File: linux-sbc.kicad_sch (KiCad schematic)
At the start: 10 parts, among them J101 Molex Mini-fit Jr

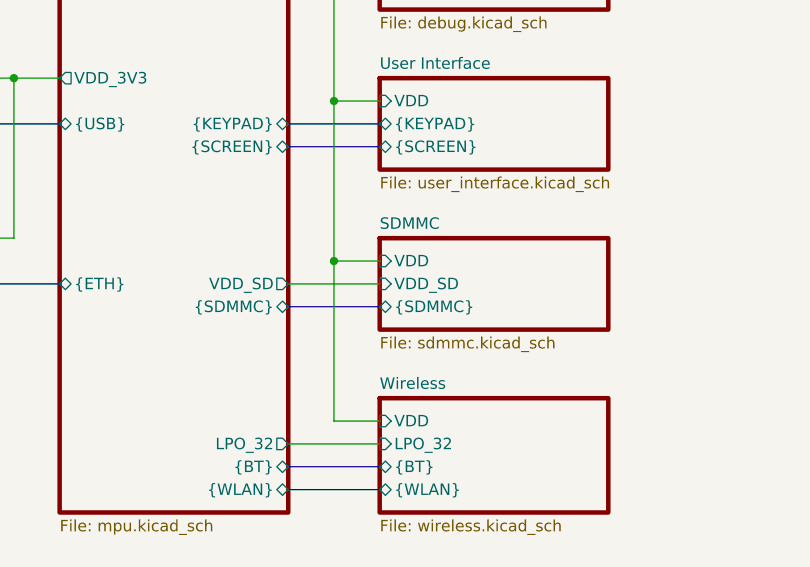
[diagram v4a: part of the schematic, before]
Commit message: Redo MPU pinout using STM32CubeMx
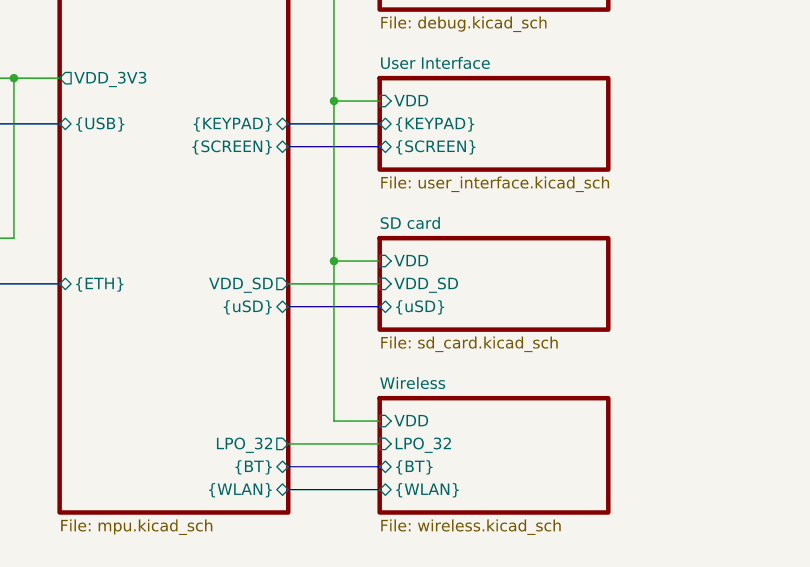
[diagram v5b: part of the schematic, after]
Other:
- sheet SDMMC renamed SD card
- sheet MPU ports: added {uSD}; removed {SDMMC}
- sheet SD card: file sdmmc.kicad_sch -> sd_card.kicad_sch
- sheet SD card ports: added {uSD}; removed {SDMMC}
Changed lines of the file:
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@@
 		(rev "v0.0.1")
 	)
-	(bus_alias "SDMMC"
-		(members "SDMMC.D[0..3]" "SDMMC.CMD" "SDMMC.CLK" "SDMMC.DET_N")
+	(bus_alias "uSD"
+		(members "uSD.D[0..3]" "uSD.CMD" "uSD.CLK" "uSD.DET_N")
 	)
 	(text "7. USB"
@@
 			(color 0 255 0 1.0000)
 		)
-		(property "Sheetname" "SDMMC"
+		(property "Sheetname" "SD card"
 			(at 252.73 165.4846 0)
 			(effects
@@
 			)
 		)
-		(property "Sheetfile" "sdmmc.kicad_sch"
+		(property "Sheetfile" "sd_card.kicad_sch"
 			(at 252.73 177.2884 0)
 			(effects
@@
 			)
 		)
-		(pin "{SDMMC}" bidirectional
+		(pin "{uSD}" bidirectional
 			(at 252.73 173.99 180)
 			(effects
@@
 			)
 		)
-		(pin "{SDMMC}" bidirectional
+		(pin "{uSD}" bidirectional
 			(at 242.57 173.99 0)
 			(effects

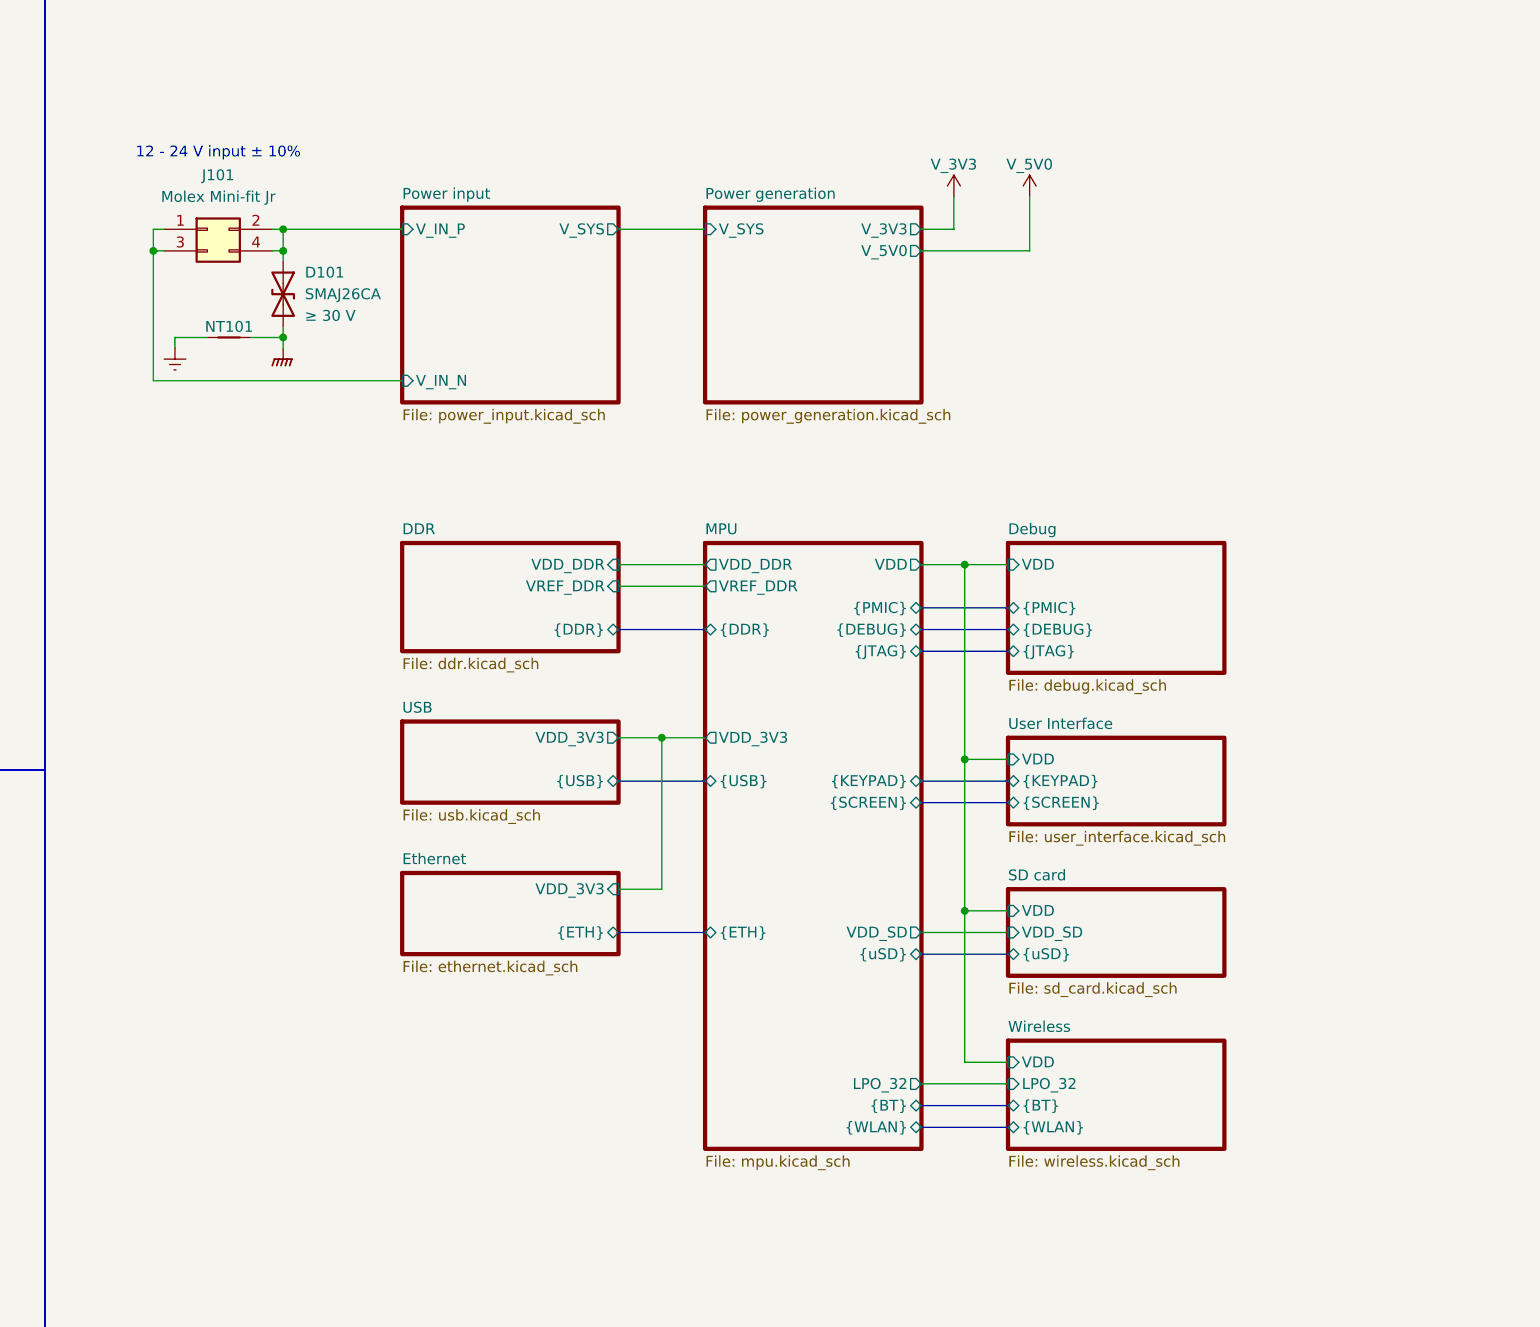
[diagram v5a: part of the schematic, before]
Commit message: Bridge chassis and gnd with 0 ohm
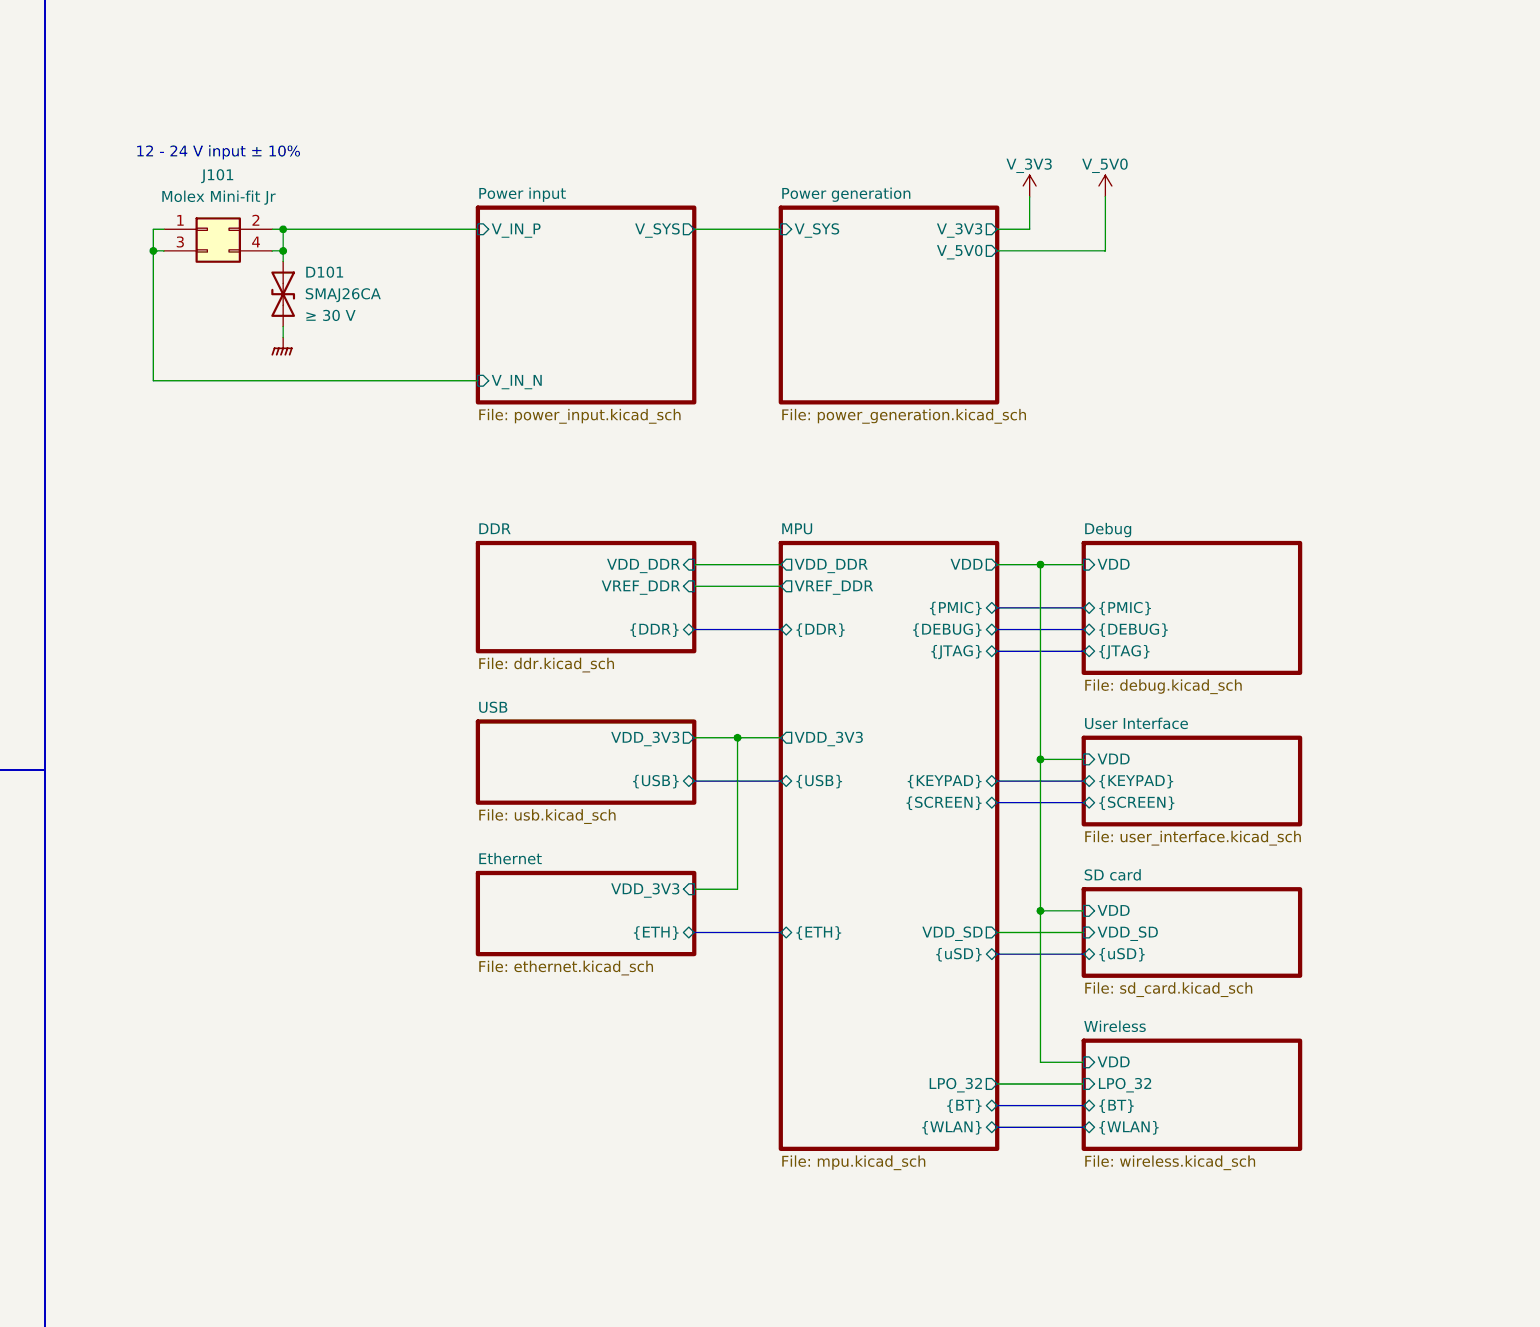
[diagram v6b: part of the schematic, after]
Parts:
- removed NT101: NetTie_2, NetTie:NetTie-2_SMD_Pad2.0mm, symbol Device:NetTie_2

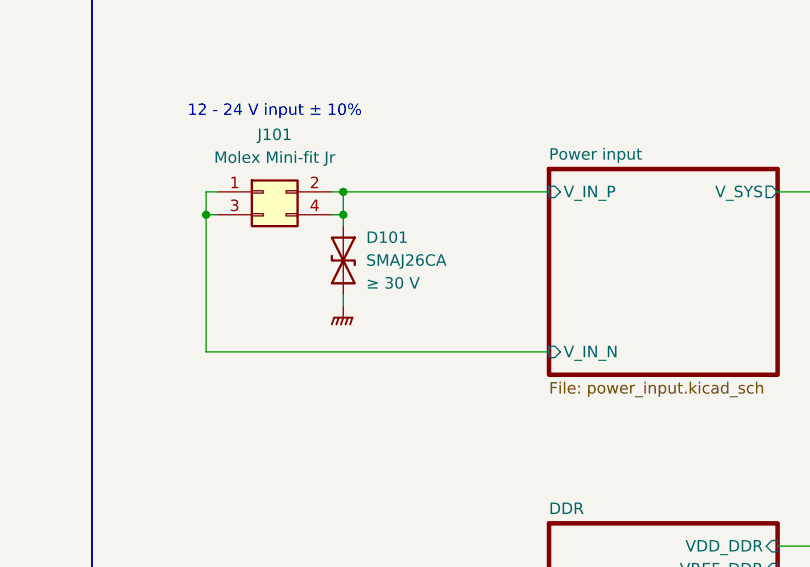
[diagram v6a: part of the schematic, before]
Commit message: Add additional info to passives
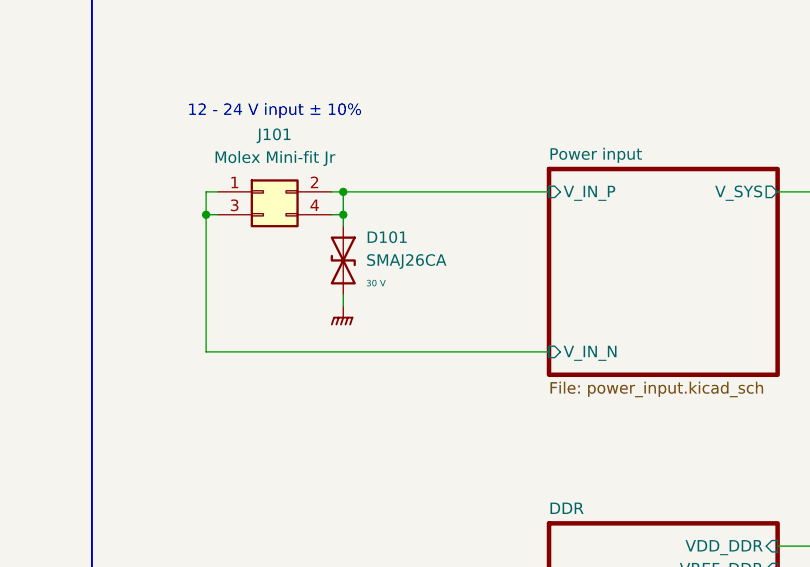
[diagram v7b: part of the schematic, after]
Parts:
- D101: Breakdown voltage ≥ 30 V -> 30 V
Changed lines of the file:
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@@
 			)
 		)
-		(property "Breakdown voltage" "≥ 30 V"
+		(property "Breakdown voltage" "30 V"
 			(at 170.18 99.06 90)
 			(effects
 				(font
-					(size 1.27 1.27)
+					(size 0.7 0.7)
 				)
 				(justify left)

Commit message: Fill BOM info
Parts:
- D101: Digi-Key Part Number (none) -> 732-SMAJ26CACT-ND
- J101: Digi-Key Part Number (none) -> 0455860005-ND
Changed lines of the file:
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@@
+			)
+		)
+		(property "Digi-Key Part Number" "0455860005-ND"
+			(at 158.75 88.9 0)
+			(effects
+				(font
+					(size 1.27 1.27)
+				)
+				(hide yes)
 			)
 		)
@@
 			)
 		)
-		(property "Datasheet" "~"
+		(property "Datasheet" "https://www.we-online.com/katalog/datasheet/824501261.pdf"
 			(at 167.64 96.52 0)
 			(effects
@@
 			)
 		)
+		(property "Digi-Key Part Number" "732-SMAJ26CACT-ND"
+			(at 167.64 96.52 90)
+			(effects
+				(font
+					(size 1.27 1.27)
+				)
+				(hide yes)
+			)
+		)
